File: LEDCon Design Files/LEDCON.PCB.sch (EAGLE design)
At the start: 24 parts

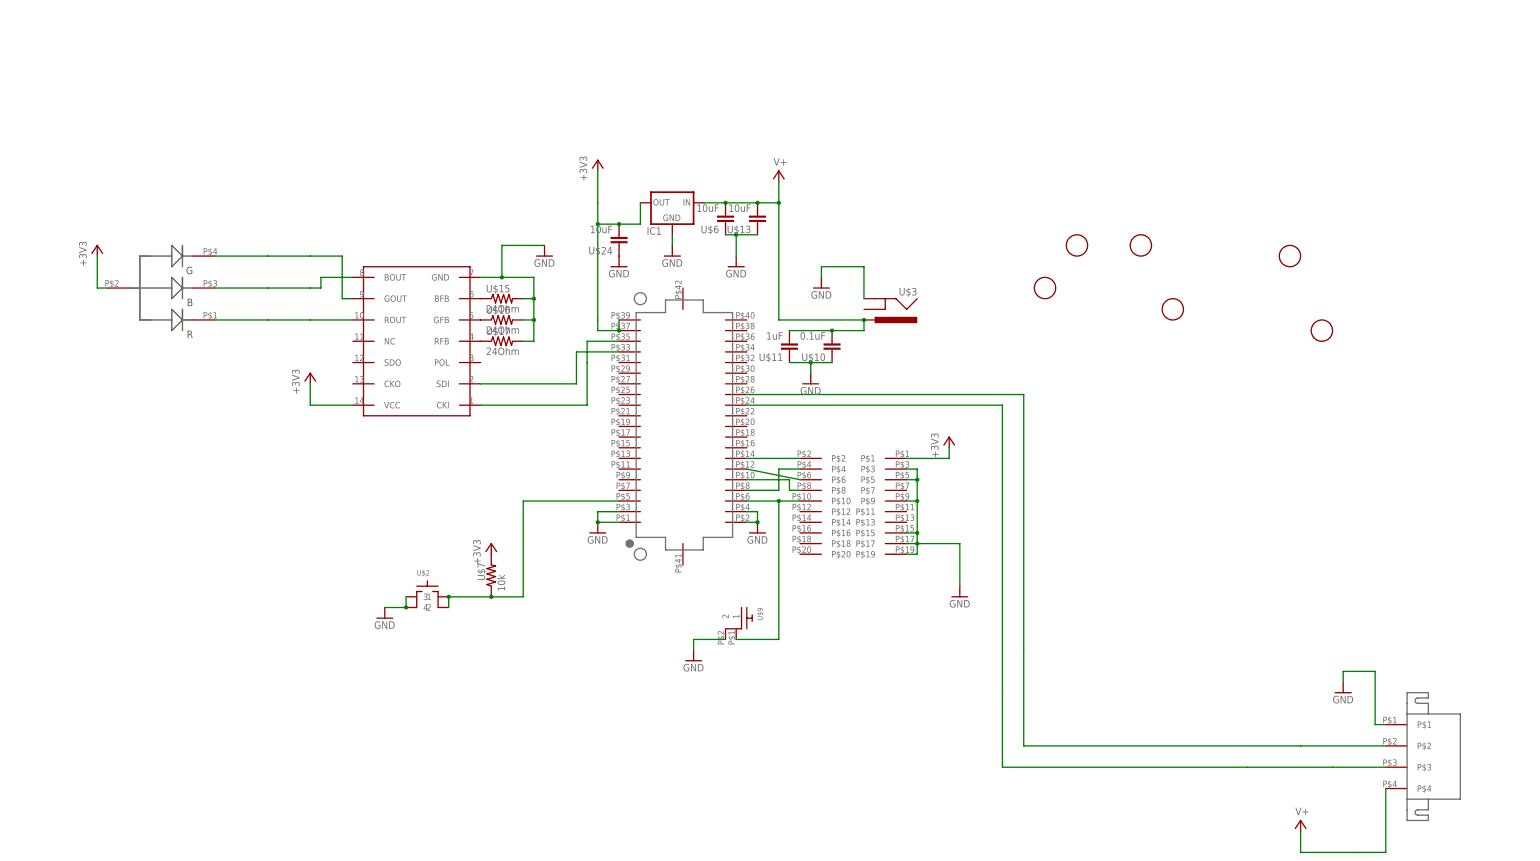
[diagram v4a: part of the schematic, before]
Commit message: Two-plane isolation version 1
All of the design changes needed to make a 2-plane isolation design.
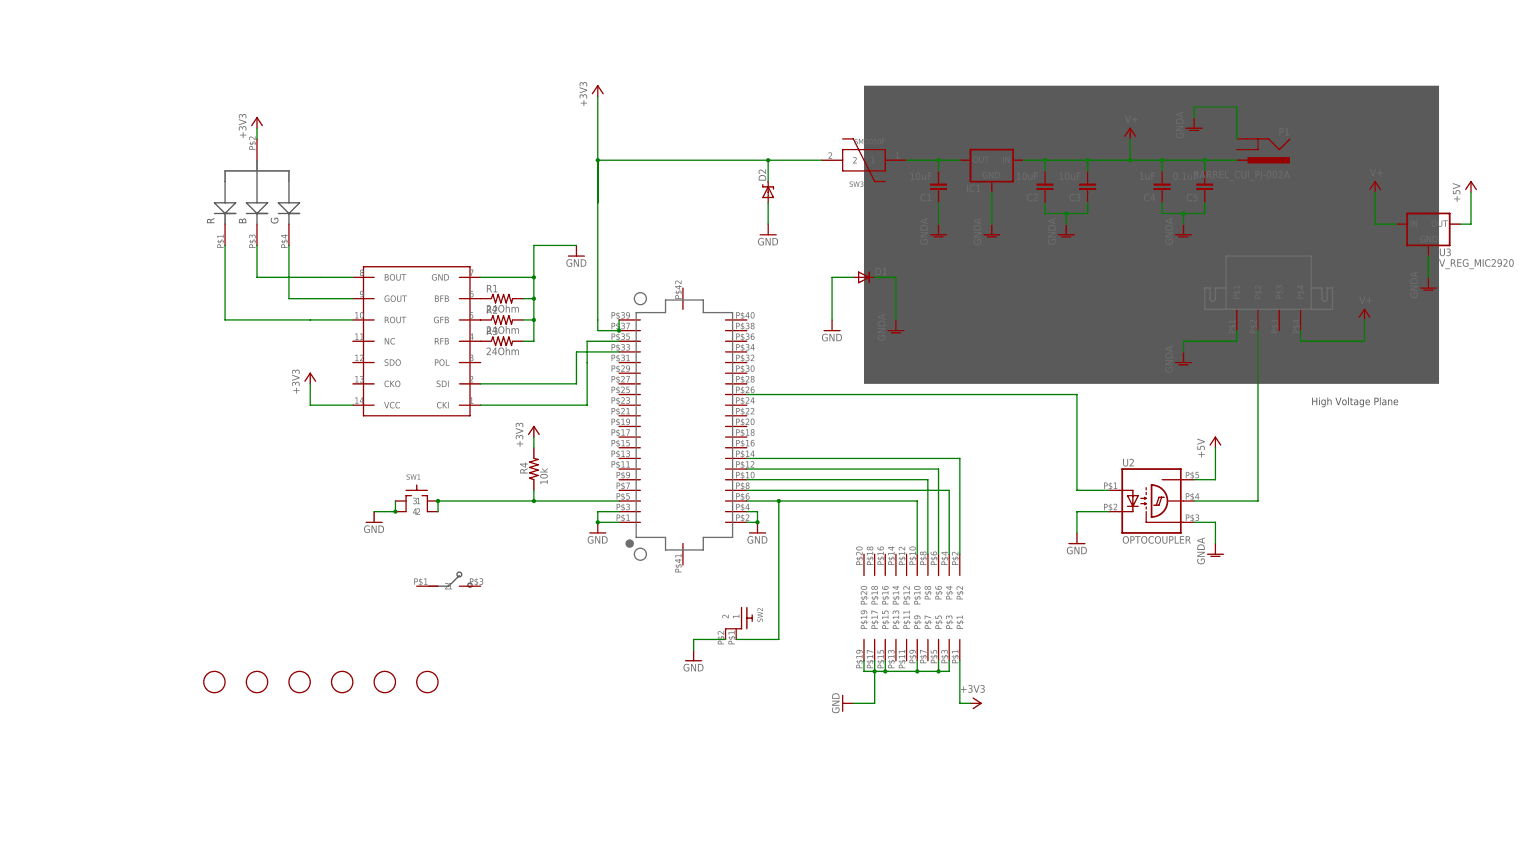
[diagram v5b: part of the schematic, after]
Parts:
- removed U$1: MATE-N-LOK_643230-1, KW2:MATE-N-LOK_643230-1
- removed U$10: 0.1uF, GW-devices:RF-C0805
- removed U$11: 1uF, GW-devices:RF-C0805
- removed U$13, U$6: 10uF, GW-devices:RF-C1210
- removed U$15, U$16, U$17: 24Ohm, GW-devices:RF-R0805
- removed U$19: 2X10JTAG, KW2:2X10JTAG
- removed U$2: SWITCH-TACTILE, GW-devices:SWITCH-TACTILE
- removed U$24: 10uF, GW-devices:RF-C0805
- removed U$3: BARREL_CUI_PJ-002A, KW2:BARREL_CUI_PJ-002A
- removed U$5: RGLBED, KW2:RGLBED
- removed U$7: 10k, GW-devices:RF-R0805
- added AWESOME: CJS, KW2:CJS
- added C1: 10uF, GW-devices:RF-C0805
- added C2, C3: 10uF, GW-devices:RF-C1210
- added C4: 1uF, GW-devices:RF-C0805
- added C5: 0.1uF, GW-devices:RF-C0805
- added D1: (no value), SparkFun:DIODESMA
- added D2: DIODE-ZENERSMB, SparkFun:DIODE-ZENERSMB
- added J1: MATE-N-LOK_643230-1, KW2:MATE-N-LOK_643230-1
- added JTAG: 2X10JTAGSMD, KW2:2X10JTAGSMD
- added LED1: RGLBED, KW2:RGLBED
- added P1: BARREL_CUI_PJ-002A, KW2:BARREL_CUI_PJ-002A
- added R1, R2, R3: 24Ohm, GW-devices:RF-R0805
- added R4: 10k, GW-devices:RF-R0805
- added SW1: SWITCH-TACTILE, GW-devices:SWITCH-TACTILE
- added SW3: SMD050F, GW-devices:SMD050F
- added U2: OPTOCOUPLER, GW-devices:OPTOCOUPLER
- added U3: V_REG_MIC2920, SparkFun:V_REG_MIC2920
- renumbered U$4 to KW2, U$8 to U1, U$9 to SW2
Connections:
- removed net CLK_5V: KW2.PTC5/LLWU_P8/SPI0_PCS0/UART1_TX/FTM0_CH3/CMP1_OUT, U$1.P$3
- removed net N$3: KW2.!RESET, SW2.1, U$19.P$10
- new net +5V: U2.VCC, U3.OUT
- new net GNDA: C1.1, C2.1, C3.1, C4.1, C5.1, D1.C, IC1.GND, J1.P$1, P1.GND, U2.GND, U3.GND
- new net N$1: C1.2, IC1.OUT, SW3.1
- new net N$2: J1.P$2, U2.OUT
- new net SW2: JTAG.P$10, KW2.!RESET, SW2.1
- net +3V3: now also D2.C, JTAG.P$1, LED1.ANODE, R4.2, SW3.2; no longer IC1.OUT, U$19.P$1, U$24.2, U$5.ANODE, U$7.2
- net DAT_5V: now also U2.A; no longer U$1.P$2
- net GND: now also D1.A, D2.A, JTAG.P$15, JTAG.P$17, JTAG.P$19, JTAG.P$3, JTAG.P$5, JTAG.P$9, R1.2, R2.2, R3.2, SW1.1, SW1.2, U2.C; no longer IC1.GND, U$1.P$1, U$10.1, U$11.1, U$13.1, U$15.2, U$16.2, U$17.2, U$19.P$15, U$19.P$17, U$19.P$19, U$19.P$3, U$19.P$5, U$19.P$9, U$2.1, U$2.2, U$24.1, U$3.GND, U$6.1
- net N$11: now also R1.1; no longer U$15.1
- net N$12: now also R2.1; no longer U$16.1
- net N$13: now also R3.1; no longer U$17.1
- net N$18: now also JTAG.P$4; no longer U$19.P$4
- net N$20: now also JTAG.P$8; no longer U$19.P$8
- net N$21: now also R4.1, SW1.3, SW1.4; no longer U$2.3, U$2.4, U$7.1
- net N$4: now also LED1.GREEN; no longer U$5.GREEN
- net N$5: now also LED1.BLUE; no longer U$5.BLUE
- net N$6: now also JTAG.P$2; no longer U$19.P$2
- net N$7: now also LED1.RED; no longer U$5.RED
- net N$8: now also JTAG.P$6; no longer U$19.P$6
- net V+: now also C2.2, C3.2, C4.2, C5.2, J1.P$4, P1.PWR, U3.IN; no longer U$1.P$4, U$10.2, U$11.2, U$13.2, U$3.PWR, U$6.2
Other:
- note added: "High Voltage Plane"
- moved on the sheet: IC1

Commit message: Redo the layout per the Codeshelf.standard DRU file
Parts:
- D1: MFGN (none) -> Diodes Inc; MFGP (none) -> B130-13-F
- D2: MFGN (none) -> On Semi; MFGP (none) -> 1SMB5913BT3G
- IC1: MFGN (none) -> Traco Power; MFGP (none) -> TSR 1-2433
- J1: MFGN (none) -> TE Connectivity; MFGP (none) -> 643230-1
- JTAG: MFGN (none) -> Sullins; MFGP (none) -> GRPB052VWQP-RC
- LED1: MFGN (none) -> Cree; MFGP (none) -> CLV1A-FKB-CK1N1G1BB7R4S3
- P1: CUI (none) -> CUI; MFGP (none) -> PJ-002A
- SW2: MFGN (none) -> TE Connectivity; MFGP (none) -> 2-1825027-0
- SW3: MFGN (none) -> TE Connectivity; MFGP (none) -> MICROSMD050F-2
- U1: MFGN (none) -> World Semi; MFGP (none) -> WS2801
- U3: MFGN (none) -> Micrel; MFGP (none) -> MIC2920A-5.0WS-TR
